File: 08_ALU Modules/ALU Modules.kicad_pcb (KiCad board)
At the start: 2 copper layers, 100 x 100 mm, 23 parts, among them J1 Flags, J2 Alu-X Bus, J3 Alu-Y Bus, J4 Alu-Out Bus, J5 Input 1, U1 74LS00, U10 74LS08, U11 74LS08, U12 74LS245, U13 74LS32, U14 74LS32, U15 74LS245, U16 74LS86, U17 74LS86, U18 74LS245, U2 74LS32, U3 74LS32, U4 74LS86, U5 74LS283, U6 74LS245, U7 74LS86, U8 74LS86, U9 74LS283

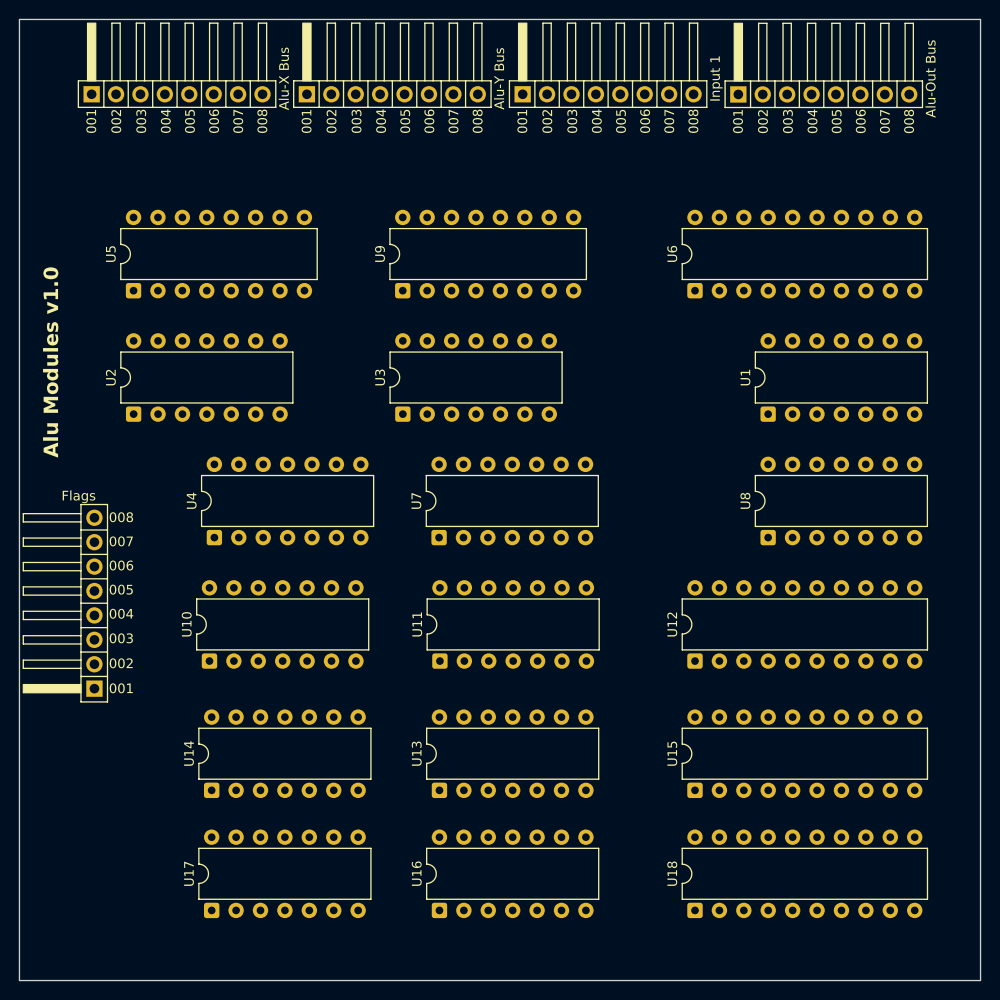
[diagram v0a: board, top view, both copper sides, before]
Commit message: Alu control and modules completed, as well as Stack pointer module
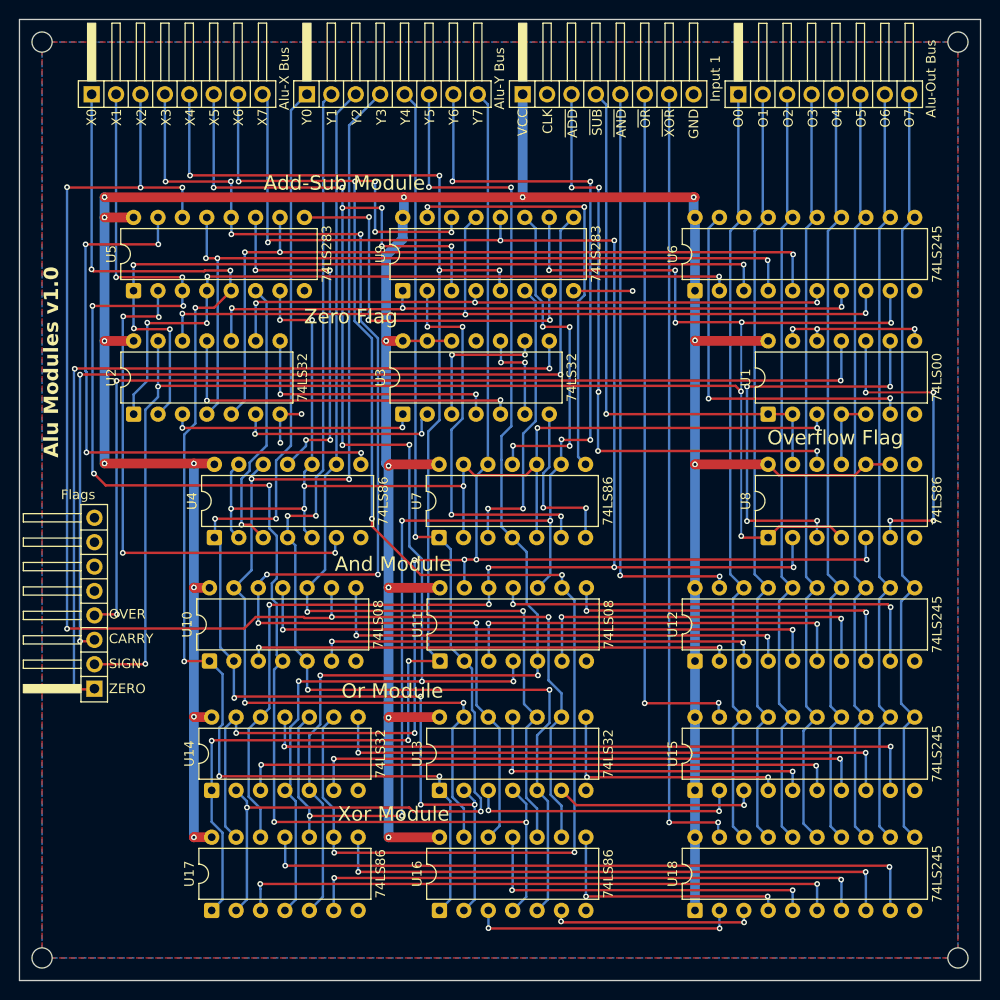
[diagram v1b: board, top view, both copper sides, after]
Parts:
- added REF**: MountingHole_2.1mm, MountingHole:MountingHole_2.1mm, F.Cu at (147.7, 147.7)
- added REF**: MountingHole_2.1mm, MountingHole:MountingHole_2.1mm, F.Cu at (52.4, 147.7)
- added REF**: MountingHole_2.1mm, MountingHole:MountingHole_2.1mm, F.Cu at (52.4, 52.4)
- added REF**: MountingHole_2.1mm, MountingHole:MountingHole_2.1mm, F.Cu at (147.7, 52.4)
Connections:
- U1 pad 4: ~{ADD} -> Net-(U1-Pad4)
- U1 pad 5: ~{SUB} -> Net-(U1-Pad4)
- U8 pad 11: unconnected-(U8-Pad11) -> Net-(U1-Pad4)
- U8 pad 12: VCC -> ~{ADD}
- U8 pad 13: VCC -> ~{SUB}
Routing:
- net VCC: track 0.00 -> 360.5 mm, vias 0 -> 18
- net SIGN: track 0.00 -> 184.1 mm, vias 0 -> 9
- net X7: track 0.00 -> 175.4 mm, vias 0 -> 8
- net X6: track 0.00 -> 166.1 mm, vias 0 -> 9
- net Y7: track 0.00 -> 153.4 mm, vias 0 -> 6
- net X5: track 0.00 -> 152.0 mm, vias 0 -> 11
- net X1: track 0.00 -> 151.0 mm, vias 0 -> 8
- net X2: track 0.00 -> 149.3 mm, vias 0 -> 6
- net X4: track 0.00 -> 144.9 mm, vias 0 -> 7
- net Y6: track 0.00 -> 139.3 mm, vias 0 -> 8
- net X3: track 0.00 -> 134.5 mm, vias 0 -> 8
- net X0: track 0.00 -> 129.8 mm, vias 0 -> 6
- net Y0: track 0.00 -> 121.1 mm, vias 0 -> 6
- net Net-(U5-C0): track 0.00 -> 120.3 mm, vias 0 -> 8
- net Y5: track 0.00 -> 119.8 mm, vias 0 -> 4
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- added copper zone on B.Cu, net GND
- added copper zone on F.Cu, net GND
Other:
- board text added: "Add-Sub Module"
- board text added: "And Module"
- board text added: "Or Module"
- board text added: "Overflow Flag"
- board text added: "Xor Module"
- board text added: "Zero Flag"

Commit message: Last revision of the cpu, all boards have been ordered. Implementation to be tested and documented in following commits.
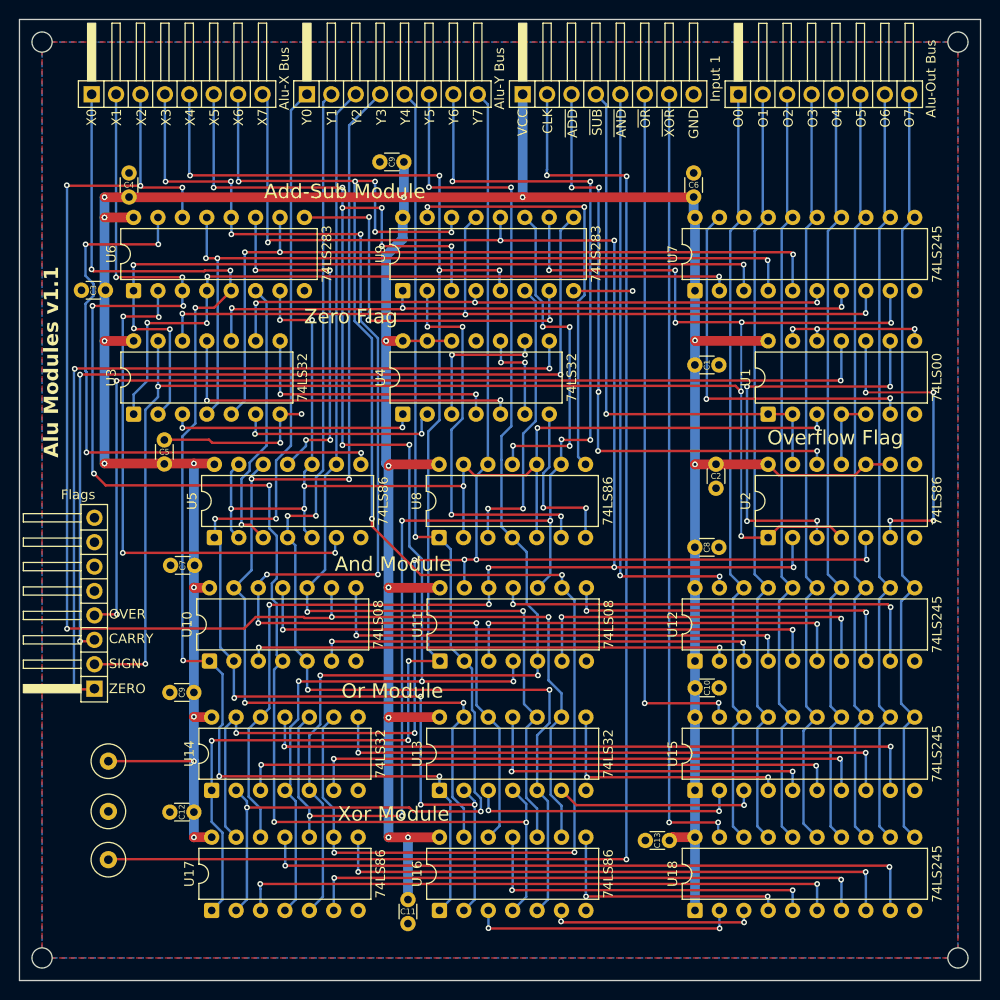
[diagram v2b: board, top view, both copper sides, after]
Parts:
- added C1: 100n, Capacitor_THT:C_Disc_D3.0mm_W1.6mm_P2.50mm, F.Cu at (120.3, 86.0)
- added C10: 100n, Capacitor_THT:C_Disc_D3.0mm_W1.6mm_P2.50mm, F.Cu at (120.3, 119.5)
- added C11: 100n, Capacitor_THT:C_Disc_D3.0mm_W1.6mm_P2.50mm, F.Cu at (90.4, 141.6)
- added C12: 100n, Capacitor_THT:C_Disc_D3.0mm_W1.6mm_P2.50mm, F.Cu at (68.2, 132.5)
- added C13: 100n, Capacitor_THT:C_Disc_D3.0mm_W1.6mm_P2.50mm, F.Cu at (117.6, 135.4)
- added C2: 100n, Capacitor_THT:C_Disc_D3.0mm_W1.6mm_P2.50mm, F.Cu at (122.5, 96.3)
- added C3: 100n, Capacitor_THT:C_Disc_D3.0mm_W1.6mm_P2.50mm, F.Cu at (59.0, 78.2)
- added C4: 100n, Capacitor_THT:C_Disc_D3.0mm_W1.6mm_P2.50mm, F.Cu at (61.4, 68.5)
- added C5: 100n, Capacitor_THT:C_Disc_D3.0mm_W1.6mm_P2.50mm, F.Cu at (65.1, 96.2)
- added C6: 100n, Capacitor_THT:C_Disc_D3.0mm_W1.6mm_P2.50mm, F.Cu at (120.2, 68.5)
- added C7: 100n, Capacitor_THT:C_Disc_D3.0mm_W1.6mm_P2.50mm, F.Cu at (68.2, 106.8)
- added C8: 100n, Capacitor_THT:C_Disc_D3.0mm_W1.6mm_P2.50mm, F.Cu at (120.3, 104.9)
- added C9: 100n, Capacitor_THT:C_Disc_D3.0mm_W1.6mm_P2.50mm, F.Cu at (68.2, 120.0)
- added C9: 100n, Capacitor_THT:C_Disc_D3.0mm_W1.6mm_P2.50mm, F.Cu at (90.0, 64.8)
- added TP1: VCC, TestPoint:TestPoint_Loop_D3.50mm_Drill0.9mm_Beaded, F.Cu at (59.2, 127.2)
- added TP2: GND, TestPoint:TestPoint_Loop_D3.50mm_Drill0.9mm_Beaded, F.Cu at (59.2, 132.4)
- added TP3: CLK, TestPoint:TestPoint_Loop_D3.50mm_Drill0.9mm_Beaded, F.Cu at (59.2, 137.4)
- renumbered J2 to J1, J3 to J2, J4 to J3, J5 to J4, J1 to J5, U8 to U2, U2 to U3, U3 to U4, U4 to U5, U5 to U6, U6 to U7, U7 to U8
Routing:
- net CLK: track 0.00 -> 141.7 mm, vias 0 -> 3
- net VCC: track 360.5 -> 382.5 mm, vias 18 -> 19
- net GND: track 28.9 -> 41.2 mm
- net Net-(U6-B3): track 61.9 -> 62.6 mm
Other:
- board text added: "Alu Modules v1.1"
- board text removed: "Alu Modules v1.0"
